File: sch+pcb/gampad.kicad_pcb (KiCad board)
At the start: 2 copper layers, 85.6 x 53.4 mm, 43 parts, among them J1 swd header, J10 Conn_01x01, J3 Conn_01x01, J4 Conn_01x01, J5 Conn_01x01, J6 Conn_01x01, J7 Conn_01x01, J8 Conn_01x01, J9 Conn_01x01, U1 STM32L442KCUx, U2 MIC5504-3.3YM5

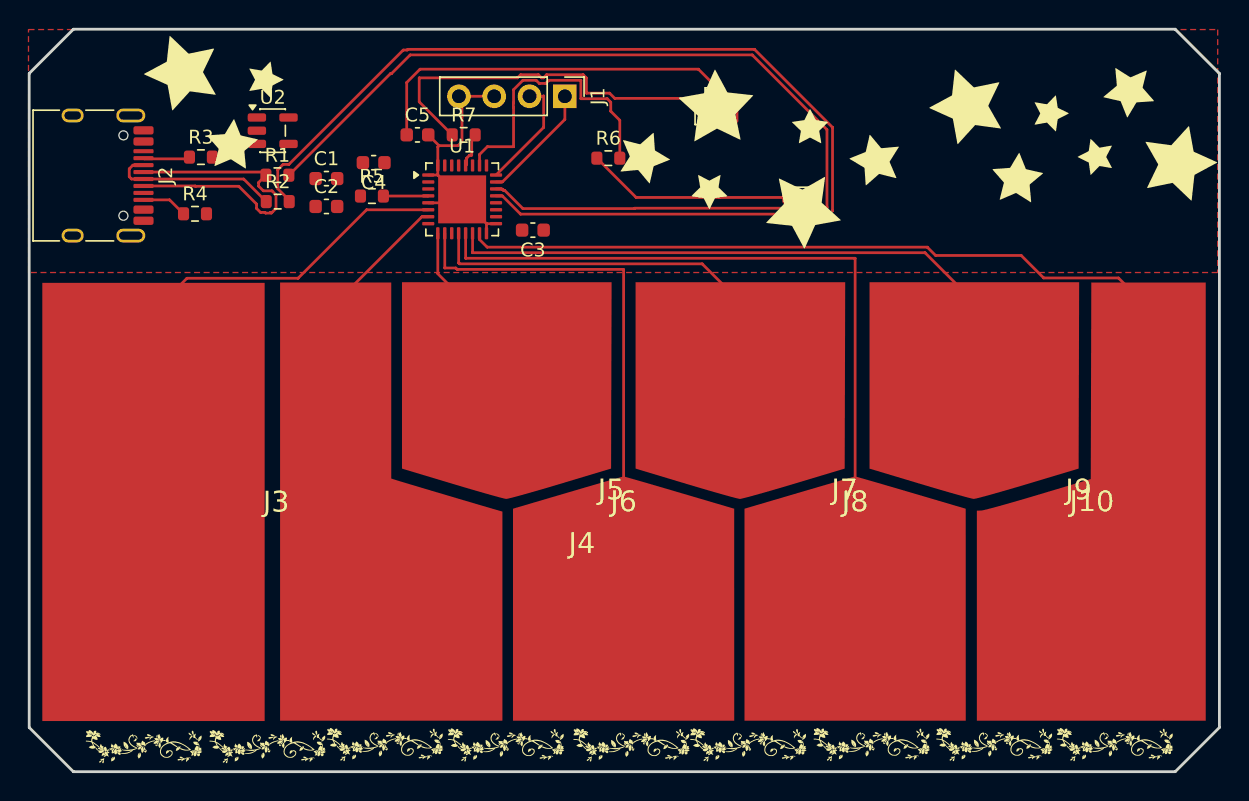
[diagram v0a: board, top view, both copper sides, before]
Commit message: updated readme and gbr files to the new stuff
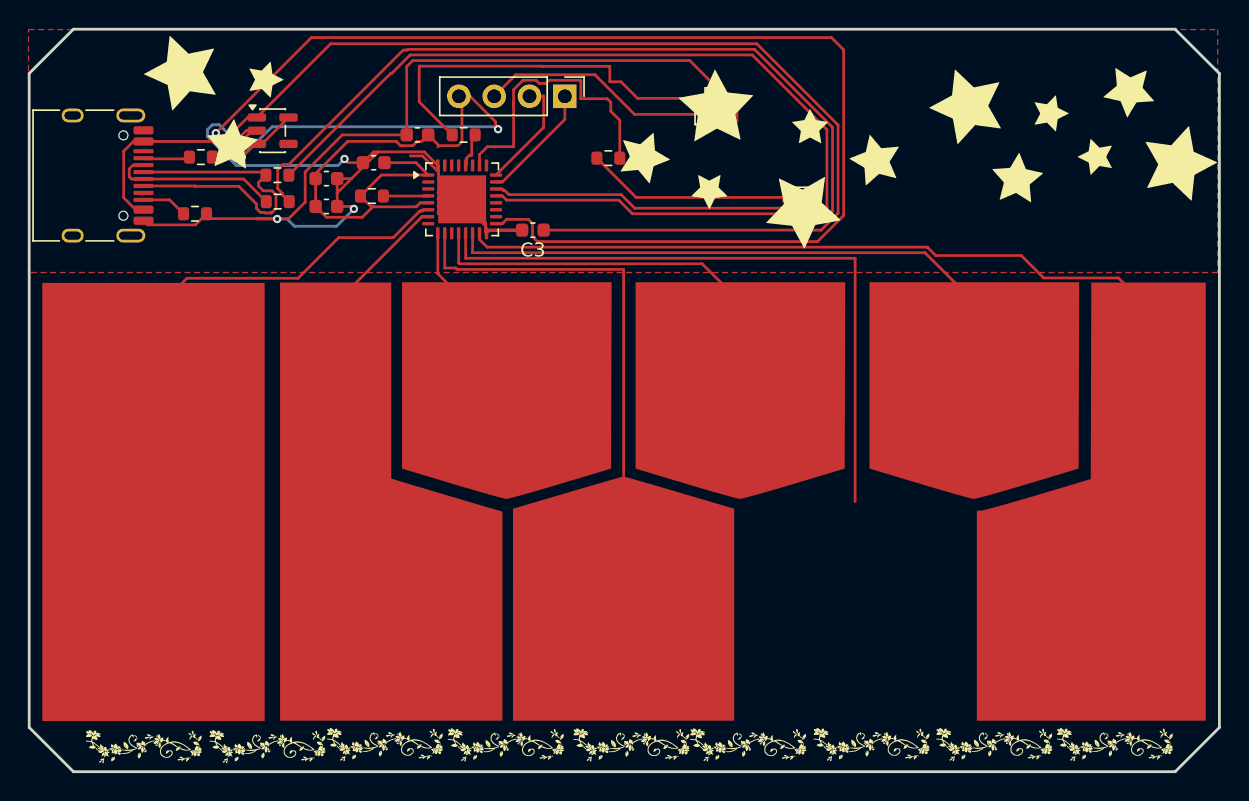
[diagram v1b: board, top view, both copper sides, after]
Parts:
- removed J8: Conn_01x01, Connector_Pin:key4
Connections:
- C1 pad 1: vin -> +3.3V
- C1 pad 2: vin -> GND
- C2 pad 1: vin -> +3.3V
- C2 pad 2: vin -> GND
- C3 pad 2: vin -> GND
- C4 pad 1: vin -> +3.3V
- C4 pad 2: vin -> GND
- C5 pad 1: vin -> GND
- C5 pad 2: vin -> +3.3V
- D1 pad 1: vin -> GND
- D2 pad 1: vin -> GND
- J1 pad 3: vin -> GND
- J1 pad 4: vin -> +3.3V
- J2 pad A1: vin -> GND
- J2 pad A12: vin -> GND
- J2 pad B1: vin -> GND
- J2 pad B12: vin -> GND
- R3 pad 2: vin -> GND
- R4 pad 2: vin -> GND
- R5 pad 1: vin -> +3.3V
- U1 pad 1: vin -> +3.3V
- U1 pad 16: vin -> GND
- U1 pad 17: vin -> +3.3V
- U1 pad 32: vin -> GND
- U1 pad 33: vin -> GND
- U1 pad 5: vin -> +3.3V
- U2 pad 2: vin -> GND
- U2 pad 3: vin -> +3.3V
- U2 pad 5: vin -> +3.3V
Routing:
- net +3.3V: track 0.00 -> 155.4 mm, vias 0 -> 3
- net GND: track 0.00 -> 141.3 mm, vias 0 -> 4
- net vin: track 53.2 -> 90.1 mm
- net Net-(D1-A): track 29.9 -> 30.7 mm
- added copper zone on F.Cu, net GND
- removed copper zone on F.Cu, net vin

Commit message: cleared the journal
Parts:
- added J8: Conn_01x01, Connector_Pin:key4, F.Cu at (122.2, 94.9)
